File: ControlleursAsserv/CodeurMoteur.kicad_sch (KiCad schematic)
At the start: 8 parts, among them J7 Codeur, J8 Motor CMD, J9 Motor FeedBack

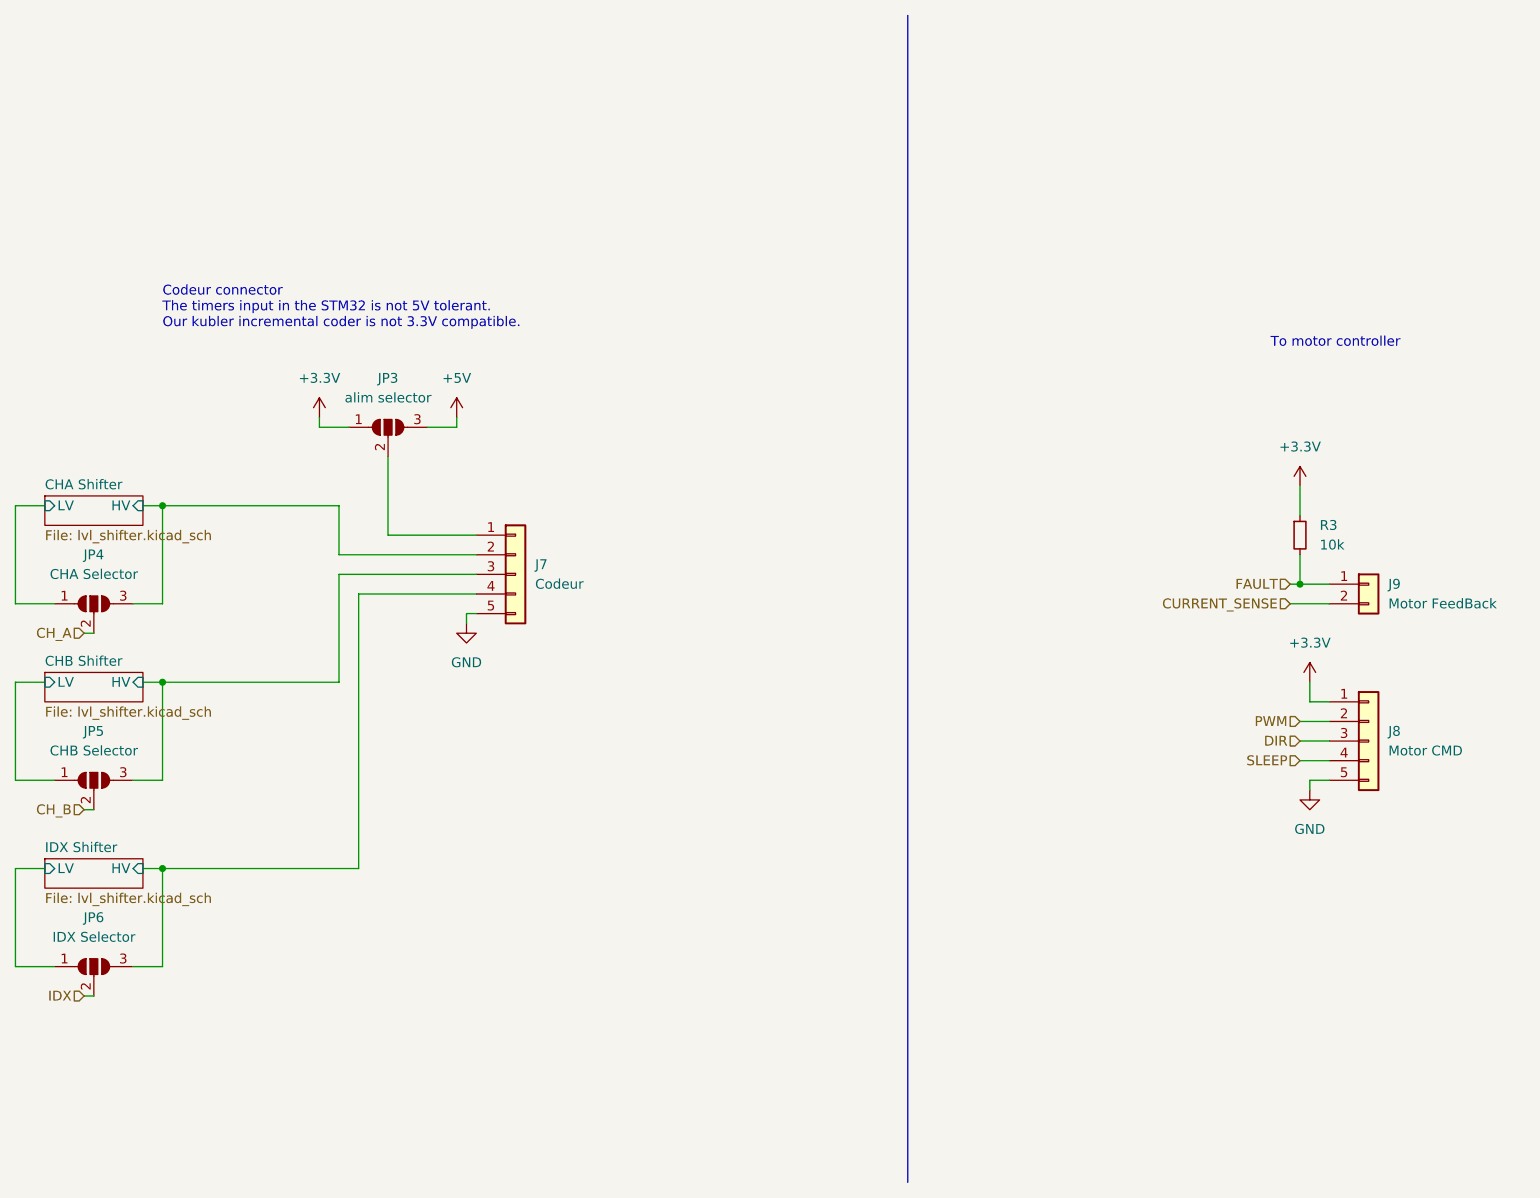
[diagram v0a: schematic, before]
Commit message: Finalize placement for AsservController
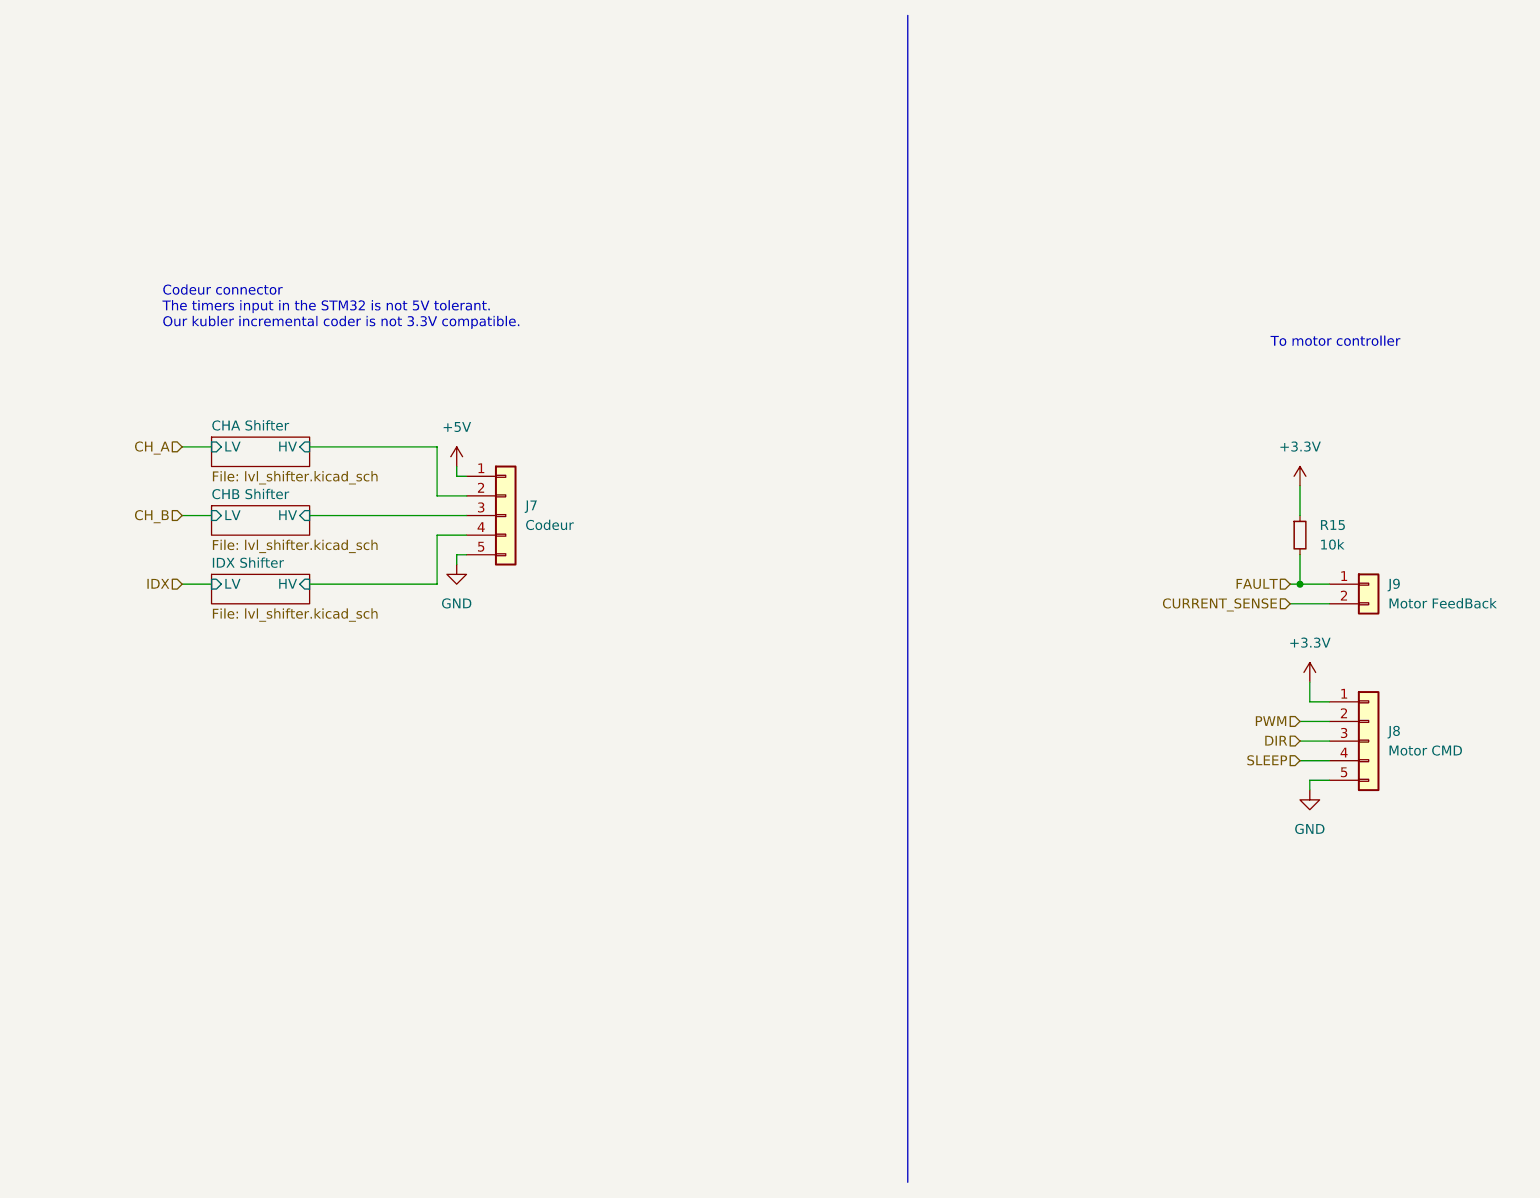
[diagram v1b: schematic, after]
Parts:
- removed JP3: alim selector, Jumper:SolderJumper-3_P1.3mm_Open_RoundedPad1.0x1.5mm, symbol Jumper:SolderJumper_3_Open
- removed JP4: CHA Selector, Jumper:SolderJumper-3_P1.3mm_Open_RoundedPad1.0x1.5mm, symbol Jumper:SolderJumper_3_Open
- removed JP5: CHB Selector, Jumper:SolderJumper-3_P1.3mm_Open_RoundedPad1.0x1.5mm, symbol Jumper:SolderJumper_3_Open
- removed JP6: IDX Selector, Jumper:SolderJumper-3_P1.3mm_Open_RoundedPad1.0x1.5mm, symbol Jumper:SolderJumper_3_Open
- J7, J8: footprint Connector_JST:JST_EH_S5B-EH_1x05_P2.50mm_Horizontal -> Connector_JST:JST_PH_S5B-PH-K_1x05_P2.00mm_Horizontal
- J9: footprint Connector_JST:JST_EH_S2B-EH_1x02_P2.50mm_Horizontal -> Connector_JST:JST_PH_S2B-PH-K_1x02_P2.00mm_Horizontal
- renumbered R3 to R15
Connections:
- net +5V: now also J7.1 (Pin_1)
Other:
- moved on the sheet: J7
